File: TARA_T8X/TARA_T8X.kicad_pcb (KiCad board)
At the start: 2 copper layers, 122.5 x 87.9 mm, 122 parts, among them J1 Screw_Terminal_01x10, J3 ESP32-WROOM-32U, J4 Conn_01x04_MountingPin, J5 Screw_Terminal_01x10, J5B1 Conn_01x06, Q1 2N5401, Q2 2N5401, Q3 2N5401, Q4 2N5401, Q5 2N5401, Q6 2N5401, Q7 2N5401, Q8 2N5401, Q9 2N5401, Q9A1 2N5401, U1 CN3903, U101 LM1117-3.3, U2 DS1307+, U3 TTL_RS485_Module, Y1 Crystal_Small

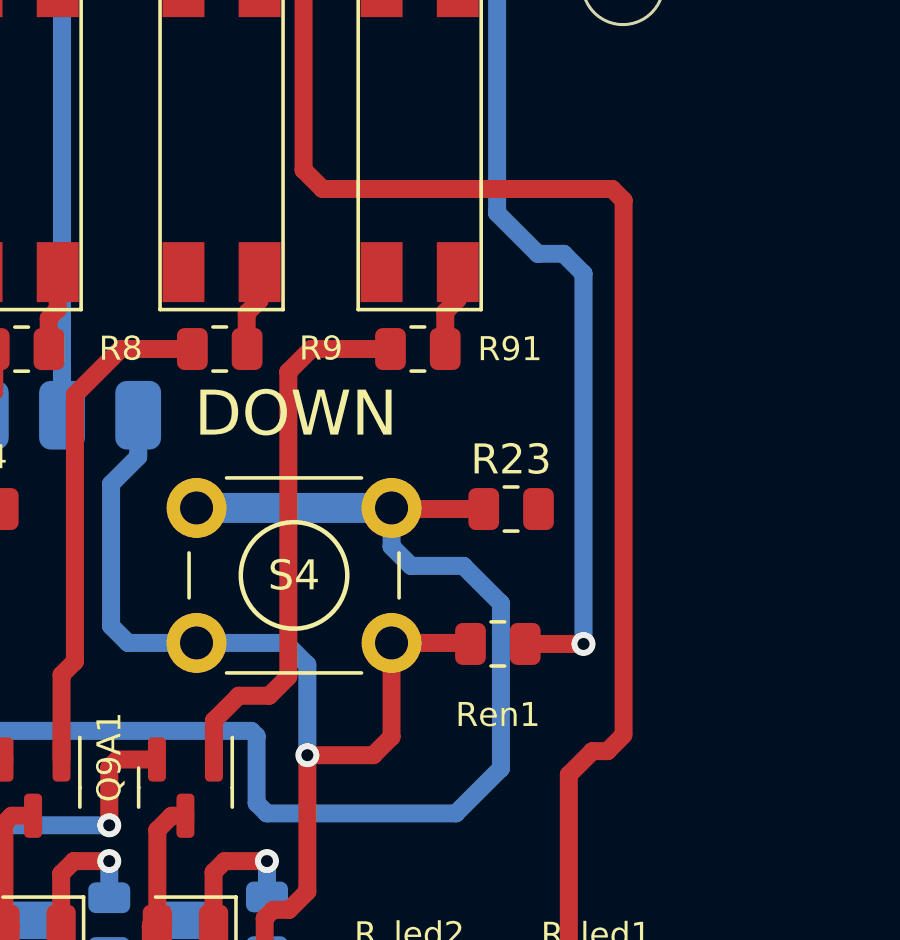
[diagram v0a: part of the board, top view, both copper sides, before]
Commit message: edit hold size S4, RL1-4 screen--> 0.8mm
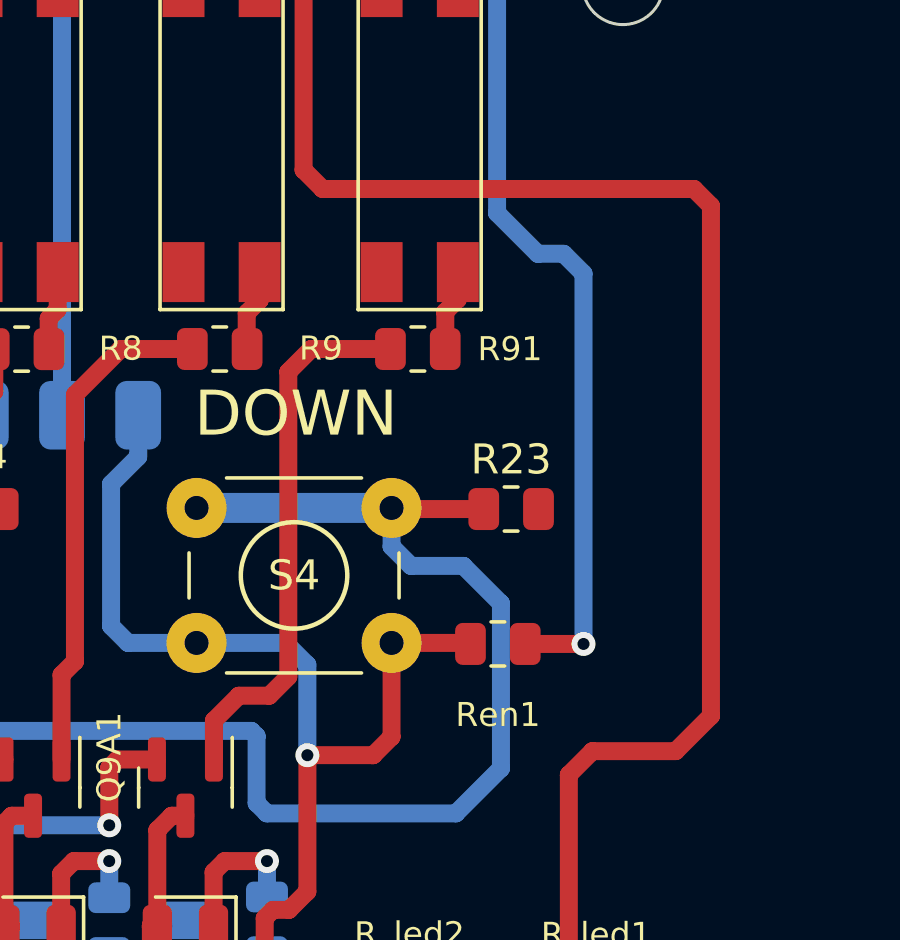
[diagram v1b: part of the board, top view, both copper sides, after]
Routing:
- net Net-(J3-Pad24): track 95.8 -> 101.1 mm
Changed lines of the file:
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@@
     (fp_line (start 0.25 -0.75) (end 3.25 -0.75) (layer "F.Fab") (width 0.1))
     (fp_circle (center 3.25 2.25) (end 1.25 2.5) (layer "F.Fab") (width 0.1) (fill none))
-    (pad "1" thru_hole circle locked (at 0 0 90) (size 2 2) (drill 1.1) (layers *.Cu *.Mask)
+    (pad "1" thru_hole circle locked (at 0 0 90) (size 2 2) (drill 0.8) (layers *.Cu *.Mask)
       (net 50 "Net-(J3-Pad7)") (pinfunction "1") (pintype "passive"))
-    (pad "1" thru_hole circle locked (at 6.5 0 90) (size 2 2) (drill 1.1) (layers *.Cu *.Mask)
+    (pad "1" thru_hole circle locked (at 6.5 0 90) (size 2 2) (drill 0.8) (layers *.Cu *.Mask)
       (net 50 "Net-(J3-Pad7)") (pinfunction "1") (pintype "passive"))
-    (pad "2" thru_hole circle locked (at 0 4.5 90) (size 2 2) (drill 1.1) (layers *.Cu *.Mask)
+    (pad "2" thru_hole circle locked (at 0 4.5 90) (size 2 2) (drill 0.8) (layers *.Cu *.Mask)
       (net 59 "/3V3") (pinfunction "2") (pintype "passive"))
-    (pad "2" thru_hole circle locked (at 6.5 4.5 90) (size 2 2) (drill 1.1) (layers *.Cu *.Mask)
+    (pad "2" thru_hole circle locked (at 6.5 4.5 90) (size 2 2) (drill 0.8) (layers *.Cu *.Mask)
       (net 59 "/3V3") (pinfunction "2") (pintype "passive"))
     (model "${KICAD6_3DMODEL_DIR}/Button_Switch_THT.3dshapes/SW_PUSH_6mm_H5mm.wrl"
@@
     (attr smd)
     (fp_text reference "RL1" (at 2.54 0 90) (layer "B.SilkS")
-      (effects (font (size 1 1) (thickness 0.15)) (justify mirror))
+      (effects (font (size 0.8 0.8) (thickness 0.15)) (justify mirror))
     )
     (fp_text value "560" (at 0 -1.65) (layer "B.Fab") hide
@@
     (attr smd)
     (fp_text reference "RL2" (at -2.5806 0.0508 90) (layer "B.SilkS")
-      (effects (font (size 1 1) (thickness 0.15)) (justify mirror))
+      (effects (font (size 0.8 0.8) (thickness 0.15)) (justify mirror))
     )
     (fp_text value "560" (at 0 -1.65) (layer "B.Fab") hide
@@
   (segment (start 174.2625 129.25) (end 174.2625 121.9625) (width 0.6) (layer "F.Cu") (net 37))
   (segment (start 165.42 101.802) (end 166.055 102.437) (width 0.6) (layer "F.Cu") (net 37))
+  (segment (start 178.437 102.437) (end 179 103) (width 0.6) (layer "F.Cu") (net 37))
   (segment (start 139.7914 70.433) (end 141.25 71.8916) (width 0.6) (layer "F.Cu") (net 37))
   (segment (start 174.2625 121.9625) (end 175.05 121.175) (width 0.6) (layer "F.Cu") (net 37))
+  (segment (start 166.055 102.437) (end 178.437 102.437) (width 0.6) (layer "F.Cu") (net 37))
   (segment (start 165.42 86.553) (end 165.42 101.802) (width 0.6) (layer "F.Cu") (net 37))
-  (segment (start 176.088 120.637) (end 176.088 120.537) (width 0.25) (layer "F.Cu") (net 37))
-  (segment (start 166.055 102.437) (end 175.707 102.437) (width 0.6) (layer "F.Cu") (net 37))
-  (segment (start 175.55 121.175) (end 176.088 120.637) (width 0.6) (layer "F.Cu") (net 37))
+  (segment (start 175.05 121.175) (end 177.825 121.175) (width 0.6) (layer "F.Cu") (net 37))
   (segment (start 141.25 71.8916) (end 141.25 83.9398) (width 0.6) (layer "F.Cu") (net 37))
   (segment (start 141.25 83.9398) (end 141.9926 84.6824) (width 0.6) (layer "F.Cu") (net 37))
-  (segment (start 176.088 102.818) (end 176.088 120.537) (width 0.6) (layer "F.Cu") (net 37))
-  (segment (start 175.707 102.437) (end 176.088 102.818) (width 0.6) (layer "F.Cu") (net 37))
   (segment (start 163.5494 84.6824) (end 165.42 86.553) (width 0.6) (layer "F.Cu") (net 37))
+  (segment (start 179 103) (end 179 120) (width 0.6) (layer "F.Cu") (net 37))
   (segment (start 137.178 70.433) (end 139.7914 70.433) (width 0.6) (layer "F.Cu") (net 37))
-  (segment (start 175.05 121.175) (end 175.55 121.175) (width 0.6) (layer "F.Cu") (net 37))
+  (segment (start 179 120) (end 177.825 121.175) (width 0.6) (layer "F.Cu") (net 37))
   (segment (start 141.9926 84.6824) (end 163.5494 84.6824) (width 0.6) (layer "F.Cu") (net 37))
   (segment (start 144.3126 68.2486) (end 144.3126 78.1038) (width 0.6) (layer "F.Cu") (net 38))

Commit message: edit new_version T8X 12-05-25
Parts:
- removed D91: 1N4007, Diode_SMD:D_1206_3216Metric
- removed LED6: LED, LED_SMD:LED_0805_2012Metric
- removed R91: 560, Resistor_SMD:R_0805_2012Metric
- removed U101: LM1117-3.3, Package_TO_SOT_SMD:SOT-223-3_TabPin2
- added C2: 100uf/16V, Capacitor_SMD:C_0805_2012Metric, F.Cu at (196.7, 94.1)
- added C3: 10uf/50v, Capacitor_SMD:C_0805_2012Metric, F.Cu at (105.0, 82.8)
- added C4: 100nF, Capacitor_SMD:C_0805_2012Metric, F.Cu at (89.9, 68.1)
- added C5: 100nF, Capacitor_SMD:C_0805_2012Metric, F.Cu at (202.8, 91.4)
- added D10: 1N4007, Diode_SMD:D_1206_3216Metric, F.Cu at (111.6, 140.1)
- added Dled1: LED, LED_SMD:LED_0805_2012Metric, F.Cu at (89.9, 71.1)
- added J2: ESP32-WROOM-32U, RF_Module:ESP32-WROOM-32U, F.Cu at (128.5, 60.2)
- added J5B1: Conn_01x06, Connector_PinHeader_2.54mm:PinHeader_1x06_P2.54mm_Vertical, F.Cu at (100.8, 45.5)
- added LED3: LED, LED_SMD:LED_0805_2012Metric, F.Cu at (138.3, 126.5)
- added OPTO14: PC817, my_footprint:SO-4_7.6x3.6mm_P2.54mm_1234, F.Cu at (173.6, 76.1)
- added R10: 560, Resistor_SMD:R_0805_2012Metric, F.Cu at (178.6, 80.7)
- added R11: 560, Resistor_SMD:R_0805_2012Metric, F.Cu at (115.5, 105.2)
- added R12: 560, Resistor_SMD:R_0805_2012Metric, F.Cu at (122.4, 105.2)
- added R13: 560, Resistor_SMD:R_0805_2012Metric, F.Cu at (89.7, 80.0)
- added R14: 560, Resistor_SMD:R_0805_2012Metric, F.Cu at (196.3, 106.6)
- added R15: 560, Resistor_SMD:R_0805_2012Metric, F.Cu at (86.4, 89.8)
- added R16: 560, Resistor_SMD:R_0805_2012Metric, F.Cu at (178.9, 83.4)
- added R17: 560, Resistor_SMD:R_0805_2012Metric, F.Cu at (157.9, 112.1)
- added R18: 560, Resistor_SMD:R_0805_2012Metric, F.Cu at (147.7, 86.8)
- added R21: 560, Resistor_SMD:R_0805_2012Metric, F.Cu at (86.3, 98.8)
- added R22: 560, Resistor_SMD:R_0805_2012Metric, F.Cu at (183.7, 115.4)
- added R23: 560, Resistor_SMD:R_0805_2012Metric, F.Cu at (86.4, 92.7)
- added R24: 560, Resistor_SMD:R_0805_2012Metric, F.Cu at (89.9, 74.1)
- added R25: 560, Resistor_SMD:R_0805_2012Metric, F.Cu at (202.6, 100.3)
- added R26: 560, Resistor_SMD:R_0805_2012Metric, F.Cu at (198.2, 120.1)
- added R27: 560, Resistor_SMD:R_0805_2012Metric, F.Cu at (199.2, 128.9)
- added R28: 560, Resistor_SMD:R_0805_2012Metric, F.Cu at (152.1, 86.7)
- added R29: 560, Resistor_SMD:R_0805_2012Metric, F.Cu at (178.7, 74.8)
- added R30: 560, Resistor_SMD:R_0805_2012Metric, F.Cu at (191.1, 104.7)
- added R31: 10K, Resistor_SMD:R_0805_2012Metric, F.Cu at (182.6, 83.4)
- added R32: 10K, Resistor_SMD:R_0805_2012Metric, F.Cu at (202.7, 120.0)
- added R33: 10K, Resistor_SMD:R_0805_2012Metric, F.Cu at (189.7, 93.5)
- added R34: 10K, Resistor_SMD:R_0805_2012Metric, F.Cu at (196.0, 115.7)
- added R35: 10K, Resistor_SMD:R_0805_2012Metric, F.Cu at (198.0, 123.1)
- added R36: 10K, Resistor_SMD:R_0805_2012Metric, F.Cu at (122.8, 77.5)
- added R37: 10K, Resistor_SMD:R_0805_2012Metric, F.Cu at (196.4, 97.6)
- added R38: 10K, Resistor_SMD:R_0805_2012Metric, F.Cu at (191.1, 101.8)
- added RF1: 0, Resistor_SMD:R_0805_2012Metric, F.Cu at (178.6, 77.8)
- added RF2: 0, Resistor_SMD:R_0805_2012Metric, F.Cu at (127.6, 79.9)
- added RL1: 560, Resistor_SMD:R_0805_2012Metric, F.Cu at (192.2, 64.5)
- added RL2: 560, Resistor_SMD:R_0805_2012Metric, F.Cu at (122.8, 74.5)
- added RL3: 560, Resistor_SMD:R_0805_2012Metric, F.Cu at (202.8, 94.4)
- added RL4: 560, Resistor_SMD:R_0805_2012Metric, F.Cu at (86.3, 95.8)
- added R_led1: 560, Resistor_SMD:R_0805_2012Metric, F.Cu at (202.6, 97.4)
- added R_led2: 560, Resistor_SMD:R_0805_2012Metric, F.Cu at (86.1, 101.7)
- added Rbo1: 10K, Resistor_SMD:R_0805_2012Metric, F.Cu at (196.3, 103.5)
- added Ren1: 560, Resistor_SMD:R_0805_2012Metric, F.Cu at (89.9, 77.1)
- added U4: DS1307+, Package_SO:SOIC-8-1EP_3.9x4.9mm_P1.27mm_EP2.29x3mm, F.Cu at (135.9, 77.3)
- C5, D1, D2, D3, D4, D5, D6, D7, D8, D9, R10, R11, R21, R22, R31, R32, R34, R35, R36, R37, R38, R39, R40, RL1, RL2, RL3, RL4, RT1, RT2: moved to F.Cu
- J3: value ESP32-WROOM-32U -> Conn_01x04_MountingPin; footprint RF_Module:ESP32-WROOM-32U -> Connector_PinHeader_2.54mm:PinHeader_1x04_P2.54mm_Vertical
- J4: value Conn_01x04_MountingPin -> Screw_Terminal_01x10; footprint Connector_PinHeader_2.54mm:PinHeader_1x04_P2.54mm_Vertical -> my_footprint:2EDGR-5.08-10P
- R19, R20: value 10K -> 560; moved to F.Cu
- U2: value DS1307+ -> LM1117-3.3; footprint Package_SO:SOIC-8-1EP_3.9x4.9mm_P1.27mm_EP2.29x3mm -> Package_TO_SOT_SMD:SOT-223-3_TabPin2; moved to F.Cu
- moved Ren1 89.6 mm to (106.0, 56.9)
- moved D8 89.3 mm to (75.1, 81.8)
- moved RT2 88.3 mm to (197.4, 56.5), turned to 0 degrees
- moved J4 87.7 mm to (191.1, 55.0)
- moved RT1 87.0 mm to (191.6, 115.8), turned to 0 degrees
- moved D6 82.8 mm to (72.6, 81.8)
- moved R4 78.1 mm to (203.6, 128.9)
- moved R9 76.6 mm to (86.1, 104.7)
- moved R2 69.8 mm to (183.6, 118.4)
- moved R19 66.2 mm to (200.6, 115.6), turned to 0 degrees
- moved D1 65.2 mm to (69.8, 82.0)
- moved CR1 60.1 mm to (69.3, 79.2), turned to 0 degrees
- moved U2 52.1 mm to (91.8, 109.0)
- moved R5 52.1 mm to (89.6, 83.0)
- moved RL3 50.9 mm to (201.5, 66.9), turned to -90 degrees
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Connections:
- J3 pad 1: GND -> Net-(J2-Pad36)
- J3 pad 2: /3V3 -> Net-(J2-Pad33)
- J3 pad 3: /EN -> /5V
- J3 pad 4: Net-(J3-Pad4) -> GND
- J4 pad 1: Net-(J3-Pad36) -> Net-(J4-Pad1)
- J4 pad 2: Net-(J3-Pad33) -> Net-(J4-Pad2)
- J4 pad 3: /5V -> Net-(J4-Pad3)
- J4 pad 4: GND -> Net-(J4-Pad4)
- LED11 pad 1: Net-(J5-Pad5) -> Net-(J4-Pad5)
- LED12 pad 1: Net-(J5-Pad5) -> Net-(J4-Pad5)
- LED13 pad 1: Net-(J5-Pad5) -> Net-(J4-Pad5)
- LED14 pad 1: Net-(J5-Pad5) -> Net-(J4-Pad5)
- OPTO10 pad 2: Net-(J5-Pad5) -> GND
- OPTO10 pad 4: Net-(J3-Pad37) -> Net-(OPTO10-Pad4)
- OPTO11 pad 2: Net-(J5-Pad5) -> Net-(J4-Pad5)
- OPTO11 pad 4: Net-(J3-Pad31) -> Net-(J2-Pad37)
- OPTO12 pad 2: Net-(J5-Pad5) -> Net-(J4-Pad5)
- OPTO12 pad 4: Net-(J3-Pad30) -> Net-(J2-Pad31)
- OPTO13 pad 2: Net-(J5-Pad5) -> Net-(J4-Pad5)
- OPTO13 pad 4: Net-(J3-Pad29) -> Net-(J2-Pad30)
- R1 pad 1: Net-(Q1-Pad1) -> Net-(LED1-Pad1)
- R1 pad 2: Net-(OPTO1-Pad4) -> GND
- R19 pad 1: Net-(OPTO10-Pad1) -> Net-(Q9-Pad1)
- R19 pad 2: Net-(J5-Pad1) -> Net-(OPTO9-Pad4)
- R2 pad 1: Net-(Q2-Pad1) -> Net-(LED2-Pad1)
- R2 pad 2: Net-(OPTO2-Pad4) -> GND
- R20 pad 1: Net-(OPTO11-Pad1) -> Net-(Q9A1-Pad1)
- R20 pad 2: Net-(J5-Pad2) -> Net-(OPTO10-Pad4)
- R3 pad 1: Net-(Q3-Pad1) -> Net-(LED3-Pad1)
- R3 pad 2: Net-(OPTO3-Pad4) -> GND
- R4 pad 1: Net-(Q4-Pad1) -> Net-(LED4-Pad1)
- R4 pad 2: Net-(OPTO4-Pad4) -> GND
- R5 pad 1: Net-(Q5-Pad1) -> Net-(LED5-Pad1)
- R5 pad 2: Net-(OPTO5-Pad4) -> GND
- R6 pad 1: Net-(Q6-Pad1) -> GND
- R6 pad 2: Net-(OPTO6-Pad4) -> Net-(LED6-Pad1)
- R7 pad 1: Net-(Q7-Pad1) -> Net-(LED7-Pad1)
- R7 pad 2: Net-(OPTO7-Pad4) -> GND
- R8 pad 1: Net-(Q8-Pad1) -> Net-(LED8-Pad1)
- R8 pad 2: Net-(OPTO8-Pad4) -> GND
- R9 pad 1: Net-(Q9-Pad1) -> Net-(LED9-Pad1)
- R9 pad 2: Net-(OPTO9-Pad4) -> GND
- RT1 pad 1: Net-(J3-Pad33) -> Net-(J2-Pad33)
- RT2 pad 1: Net-(J3-Pad36) -> Net-(J2-Pad36)
- S1 pad 1: Net-(J3-Pad4) -> Net-(J2-Pad4)
- S2 pad 1: Net-(J3-Pad5) -> Net-(J2-Pad6)
- S3 pad 1: Net-(J3-Pad6) -> Net-(J2-Pad7)
- S4 pad 1: Net-(J3-Pad7) -> Net-(J2-Pad5)
- U2 pad 1: Net-(U2-Pad1) -> GND
- U2 pad 2: Net-(U2-Pad2) -> /3V3
- U2 pad 3: Net-(BT1-Pad1) -> /5V
- Y1 pad 1: Net-(U2-Pad1) -> Net-(U4-Pad1)
- Y1 pad 2: Net-(U2-Pad2) -> Net-(U4-Pad2)
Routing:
- net /3V3: track 317.8 -> 155.0 mm, vias 5 -> 4
- net /VCC: track 171.2 -> 20.5 mm, vias 14 -> 6
- net /VCC2: track 108.9 -> 0.00 mm, vias 2 -> 0
- net /EN: track 159.8 -> 54.0 mm, vias 4 -> 3
- net /5V: track 90.5 -> 0.00 mm
- net Net-(J4-Pad5): track 0.00 -> 82.4 mm
- net /A: track 78.1 -> 0.00 mm
- net Net-(J3-Pad37): track 73.2 -> 0.00 mm, vias 2 -> 0
- net Net-(J5-Pad5): track 68.7 -> 0.00 mm
- net Net-(J3-Pad7): track 103.5 -> 36.2 mm, vias 3 -> 1
- net Net-(J3-Pad26): track 55.5 -> 0.00 mm
- net Net-(J3-Pad31): track 52.8 -> 0.00 mm
- net Net-(J2-Pad37): track 0.00 -> 45.7 mm
- net Net-(J3-Pad36): track 45.6 -> 0.00 mm, vias 3 -> 0
- net Net-(J3-Pad6): track 55.0 -> 9.53 mm, vias 1 -> 0
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- removed copper zone on B.Cu, net GND
- removed copper zone on F.Cu, net GND
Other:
- outline, holes or cut-outs redrawn

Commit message: ล่าสุดวันเสาร์ที่4ตุลาคม68
rer
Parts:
- removed the Dled1 at (182.5, 132.4)
- removed J5: Screw_Terminal_01x10, my_footprint:2EDGR-5.08-10P
- removed J5B1 (x2): Conn_01x06, Connector_PinHeader_2.54mm:PinHeader_1x06_P2.54mm_Vertical
- removed the LED3 at (133.2, 126.5)
- removed OPTO91: PC817, my_footprint:SO-4_7.6x3.6mm_P2.54mm_1234
- removed the R10 at (111.5, 98.8)
- removed the R10 at (178.6, 80.7)
- removed the R11 at (115.5, 105.2)
- removed the R11 at (118.6, 98.8)
- removed the R12 at (122.4, 105.2)
- removed the R12 at (125.5, 98.8)
- removed the R13 at (132.4, 98.8)
- removed the R14 at (139.3, 98.8)
- removed the R15 at (146.2, 98.8)
- removed the R16 at (153.0, 98.8)
- removed the R17 at (157.9, 112.1)
- removed the R17 at (159.9, 98.8)
- removed the R18 at (147.7, 86.8)
- removed the R18 at (166.6, 98.8)
- removed R181: 560, Resistor_SMD:R_0805_2012Metric
- removed the R21 at (162.8, 66.5)
- removed the R23 at (179.7, 112.6)
- removed the R25 at (144.0, 112.6)
- removed the R25 at (202.6, 100.3)
- removed the R26 at (126.0, 112.6)
- removed the R26 at (198.2, 120.1)
- removed the R32 at (102.7, 109.5)
- removed the R32 at (202.7, 120.0)
- removed the R33 at (106.0, 103.3)
- removed the R34 at (140.8, 126.4)
- removed the R34 at (196.0, 115.7)
- removed the R35 at (146.0, 126.4)
- removed the R35 at (198.0, 123.1)
- removed the R36 at (151.0, 126.4)
- removed the R37 at (196.4, 97.6)
- removed the R37 at (156.1, 126.4)
- removed the RL1 at (181.5, 71.1)
- removed the RL2 at (182.2, 79.1)
- removed the R_led1 at (182.5, 128.7)
- removed the R_led1 at (202.6, 97.4)
- removed the R_led2 at (176.3, 128.7)
- added LED6: LED, LED_SMD:LED_0805_2012Metric, F.Cu at (148.6, 126.5)
- added R10: 560, Resistor_SMD:R_0805_2012Metric, F.Cu at (168.6, 123.8)
- added R11: 560, Resistor_SMD:R_0805_2012Metric, F.Cu at (119.5, 84.9)
- added R12: 560, Resistor_SMD:R_0805_2012Metric, F.Cu at (119.5, 100.2)
- added R17: 560, Resistor_SMD:R_0805_2012Metric, F.Cu at (157.1, 101.6)
- added R18: 560, Resistor_SMD:R_0805_2012Metric, F.Cu at (164.6, 101.5)
- added R25: 560, Resistor_SMD:R_0805_2012Metric, F.Cu at (211.7, 51.5)
- added R26: 560, Resistor_SMD:R_0805_2012Metric, F.Cu at (216.1, 45.6)
- added R32: 10K, Resistor_SMD:R_0805_2012Metric, F.Cu at (221.8, 79.0)
- added R34: 10K, Resistor_SMD:R_0805_2012Metric, F.Cu at (195.5, 66.4)
- added R35: 10K, Resistor_SMD:R_0805_2012Metric, F.Cu at (221.8, 82.0)
- added R37: 10K, Resistor_SMD:R_0805_2012Metric, F.Cu at (226.2, 67.2)
- added R_led1: 560, Resistor_SMD:R_0805_2012Metric, F.Cu at (182.2, 128.9)
- J2: footprint RF_Module:ESP32-WROOM-32U -> RF_Module:ESP32-S3-WROOM-1
- RF2: value 0 -> 0
- moved R23 142.8 mm to (219.3, 40.6), turned to 180 degrees
- moved R24 124.4 mm to (211.7, 48.6)
- moved C5 114.4 mm to (92.5, 61.0)
- moved Dled1 111.0 mm to (182.5, 132.4)
- moved R_led2 94.1 mm to (176.2, 128.9)
- moved RL3 93.1 mm to (114.3, 65.2)
- moved D7 88.2 mm to (104.6, 126.3), turned to 180 degrees
- moved R27 82.1 mm to (216.1, 48.6)
- moved R9 80.0 mm to (163.8, 123.8), turned to 180 degrees
- moved R28 73.0 mm to (216.1, 51.5)
- moved RL3 70.3 mm to (131.3, 64.0)
- moved R5 69.3 mm to (143.6, 126.5)
- moved R22 68.2 mm to (119.3, 93.0), turned to -90 degrees
- moved J2 66.6 mm to (192.4, 78.9), turned to -90 degrees
- moved R4 65.6 mm to (138.1, 126.5)
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- renumbered Q9A1 to Q10
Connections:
- net Net-(J2-Pad26) renamed /IO04
- J2 pad 34: Net-(J2-Pad34) -> unconnected-(J2-RXD0/IO3-Pad34)
- J2 pad 35: Net-(J2-Pad35) -> unconnected-(J2-TXD0/IO1-Pad35)
- LED1 pad 1: Net-(LED1-Pad1) -> Net-(LED1-K)
- LED10 pad 1: Net-(LED10-Pad1) -> Net-(LED10-K)
- LED13 pad 2: Net-(LED13-Pad2) -> Net-(LED13-A)
- LED14 pad 2: Net-(LED14-Pad2) -> Net-(LED14-A)
- LED8 pad 1: Net-(LED8-Pad1) -> Net-(LED8-K)
- LED9 pad 1: Net-(LED9-Pad1) -> Net-(LED9-K)
- R1 pad 1: Net-(LED1-Pad1) -> Net-(LED1-K)
- R8 pad 1: Net-(LED8-Pad1) -> Net-(LED8-K)
- R9 pad 1: Net-(LED9-Pad1) -> Net-(LED9-K)
- RL3 pad 2: Net-(LED13-Pad2) -> Net-(LED13-A)
- RL4 pad 2: Net-(LED14-Pad2) -> Net-(LED14-A)
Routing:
- net /BOOT: track 96.1 -> 0.00 mm, vias 3 -> 0
- net Net-(J3-Pad24): track 93.7 -> 0.00 mm
- net /3V3: track 155.0 -> 63.8 mm, vias 4 -> 0
- net Net-(J4-Pin_5): track 82.4 -> 0.00 mm
- net Net-(D4-K): track 0.00 -> 77.5 mm, vias 0 -> 3
- net Net-(D5-K): track 10.7 -> 86.5 mm, vias 0 -> 1
- net Net-(D6-K): track 10.8 -> 82.1 mm, vias 0 -> 3
- net Net-(D3-K): track 3.19 -> 73.8 mm, vias 0 -> 3
- net Net-(J3-Pad23): track 68.7 -> 0.00 mm, vias 2 -> 0
- net Net-(D10-K): track 10.7 -> 76.3 mm
- net Net-(J3-Pad16): track 64.7 -> 0.00 mm, vias 2 -> 0
- net Net-(D9-K): track 9.81 -> 71.6 mm
- net Net-(D8-K): track 10.8 -> 67.4 mm
- net Net-(J3-Pad14): track 55.8 -> 0.00 mm, vias 2 -> 0
- net /EN: track 54.0 -> 0.00 mm, vias 3 -> 0
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- added copper zone on B.Cu, net GND
- added copper zone on F.Cu, net GND
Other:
- outline, holes or cut-outs redrawn
- board text removed: "V2.8.3"

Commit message: 202510041905
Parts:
- moved RL3 5.48 mm to (113.7, 59.8)
- moved Ren1 3.80 mm to (119.8, 61.5)
- moved C3 2.78 mm to (118.8, 65.0)
- moved R6 2.75 mm to (148.4, 126.5), turned to 180 degrees
- moved R7 2.75 mm to (153.5, 126.5), turned to 0 degrees
- moved LED7 2.52 mm to (153.6, 124.0)
- moved LED6 2.50 mm to (148.4, 124.0)
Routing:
- net Net-(D7-K): track 63.3 -> 56.9 mm
- net Net-(LED6-K): track 0.00 -> 4.17 mm
- net Net-(D6-K): track 82.1 -> 83.5 mm

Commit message: 202506100619_home_win10_kicad9
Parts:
- moved D1 3.10 mm to (104.6, 106.7)
- moved D2 2.75 mm to (104.6, 109.8)
- moved D3 2.40 mm to (104.6, 112.9)
- moved D4 2.05 mm to (104.6, 116.0)
- moved D5 1.80 mm to (104.6, 119.0)
- moved D6 1.50 mm to (104.6, 122.1)
- moved D7 1.15 mm to (104.6, 125.2)
- moved D8 0.70 mm to (104.6, 128.3)
- moved D9 0.35 mm to (104.6, 131.4)
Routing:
- net Net-(D1-K): track 54.9 -> 58.0 mm
- net Net-(D2-K): track 49.9 -> 52.7 mm
- net Net-(D3-K): track 73.8 -> 76.2 mm
- net Net-(D4-K): track 77.5 -> 79.6 mm
- net Net-(D5-K): track 86.5 -> 88.1 mm
- net Net-(D6-K): track 83.5 -> 85.0 mm
- net Net-(D7-K): track 56.9 -> 58.1 mm
- removed copper zone on B.Cu, net GND
- removed copper zone on F.Cu, net GND

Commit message: 202510060643
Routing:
- added copper zone on B.Cu, net GND
- added copper zone on F.Cu, net GND
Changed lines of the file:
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@@
 		)
 		(fill no)
+		(locked yes)
 		(layer "F.SilkS")
 	)
@@
 		(net 114)
 	)
+	(zone
+		(net 1)
+		(net_name "GND")
+		(layers "F.Cu" "B.Cu")
+		(hatch edge 0.5)
+		(connect_pads
+			(clearance 0.508)
+		)
+		(min_thickness 0.25)
+		(filled_areas_thickness no)
+		(fill yes
+			(thermal_gap 0.5)
+			(thermal_bridge_width 0.5)
+		)
+		(polygon
+			(pts
+				(xy 84.8 50.3) (xy 207 50.2) (xy 207 57.3) (xy 199.1 57.3) (xy 199.075 69.125) (xy 199.15 88.725)
+				(xy 207 88.725) (xy 207 137.825) (xy 84.65 137.825)
+			)
+		)
+	)
 	(embedded_fonts no)

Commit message: 20251006_grennsave_win10_kicad9
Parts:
- moved C2 24.5 mm to (108.6, 83.6)
- moved C1 13.4 mm to (95.5, 103.9), turned to 180 degrees
- moved R31 8.97 mm to (100.5, 99.2)
- moved U2 6.88 mm to (93.1, 115.8)
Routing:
- net /3V3: track 63.8 -> 104.6 mm, vias 0 -> 1
- net Net-(Dled1-A): track 0.00 -> 3.63 mm
- net Net-(Dled2-A): track 0.00 -> 3.52 mm
